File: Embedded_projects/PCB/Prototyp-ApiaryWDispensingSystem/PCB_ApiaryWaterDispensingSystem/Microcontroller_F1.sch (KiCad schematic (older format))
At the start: 47 parts, among them J4 Conn_01x06

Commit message: F1 completed
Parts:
- added C10: 20pF, symbol Device:C
- added J1, J4, J?: Conn_02x01, symbol Connector_Generic:Conn_02x01
- added JP16, JP? (x2): Jumper_2_Open, symbol Jumper:Jumper_2_Open
- added R2, R3: 10k, symbol Device:R
- added R23, R27, R4: 4k7, symbol Device:R
- added R24, R25: 100, symbol Device:R
- added R26: [N/A], symbol Device:R
- added R6: 100k, symbol Device:R
- added R7: 2k7, symbol Device:R
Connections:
- net +3V3: now also J1.1 (Pin_1), R23.1, R26.2
- net +5VA: now also R7.2
- net AIN_1: now also U?.10 (PA0), R23.2, R27.2
- net GND: now also U?.20 (PB2), U?.23 (VSS), U?.35 (VSS), U?.47 (VSS), U?.8 (VSSA), C10.2, J4.1 (Pin_1), R2.1, R27.1, R3.1, R4.1, R6.2
- net STM_JTCK: now also U?.37 (PA14)
- net STM_JTMS: now also U?.34 (PA13)
- net T_JTCK: now also U?.15 (PA5), U?.26 (PB13)
- net T_JTMS: now also U?.27 (PB14), R24.1
- net T_NRST: now also U?.18 (PB0)
- net T_SWO: now also U?.31 (PA10)
- net USB_DM: now also U?.32 (PA11)
- net USB_DP: now also U?.33 (PA12)
- net USB_RENUMn: now also U?.38 (PA15)
- net OSC_OUT: now reaches C?.2, U?.6 (PD1), Y?.1
- net OSC_IN: now reaches C3.2, U?.5 (PD0), Y?.2
- net ST_LINK_TX: now reaches U?.12 (PA2)
- net ST_LINK_TX: now also J?.1 (Pin_1), JP?.1 (A)
- net ST_LINK_RX: now reaches U?.13 (PA3)
- net ST_LINK_RX: now also J?.2 (Pin_2), JP?.1 (A)
- net T_JTDO: now reaches U?.16 (PA6)
- net T_JTDI: now reaches U?.17 (PA7)
- net at U?.2 (PC13): now also R3.2
- net at U?.21 (PB10): now also J4.2 (Pin_2), R26.1
- net T_SWDIO_IN: now reaches U?.25 (PB12)
- net T_SWDIO_IN: now also R24.2
- net PWR_ENn: now reaches U?.28 (PB15)
- net PWR_ENn: now also J1.2 (Pin_2), R4.2, R7.1
- net at U?.29 (PA8): now also R25.2
- net at U?.3 (PC14): now also R2.2
- net LED_STLINK: now reaches U?.30 (PA9)
- net PWR_EXT: now reaches U?.39 (PB3)
- net BOOT0: now reaches U?.44 (BOOT0)
- net BOOT0: now also R6.1
- new net: C10.1, JP16.1 (A), R25.1
- new net MCO: JP16.2 (B)
- new net STLK_RX: JP?.2 (B)
- new net STLK_TX: JP?.2 (B)
- no-connect marks 1 -> 11

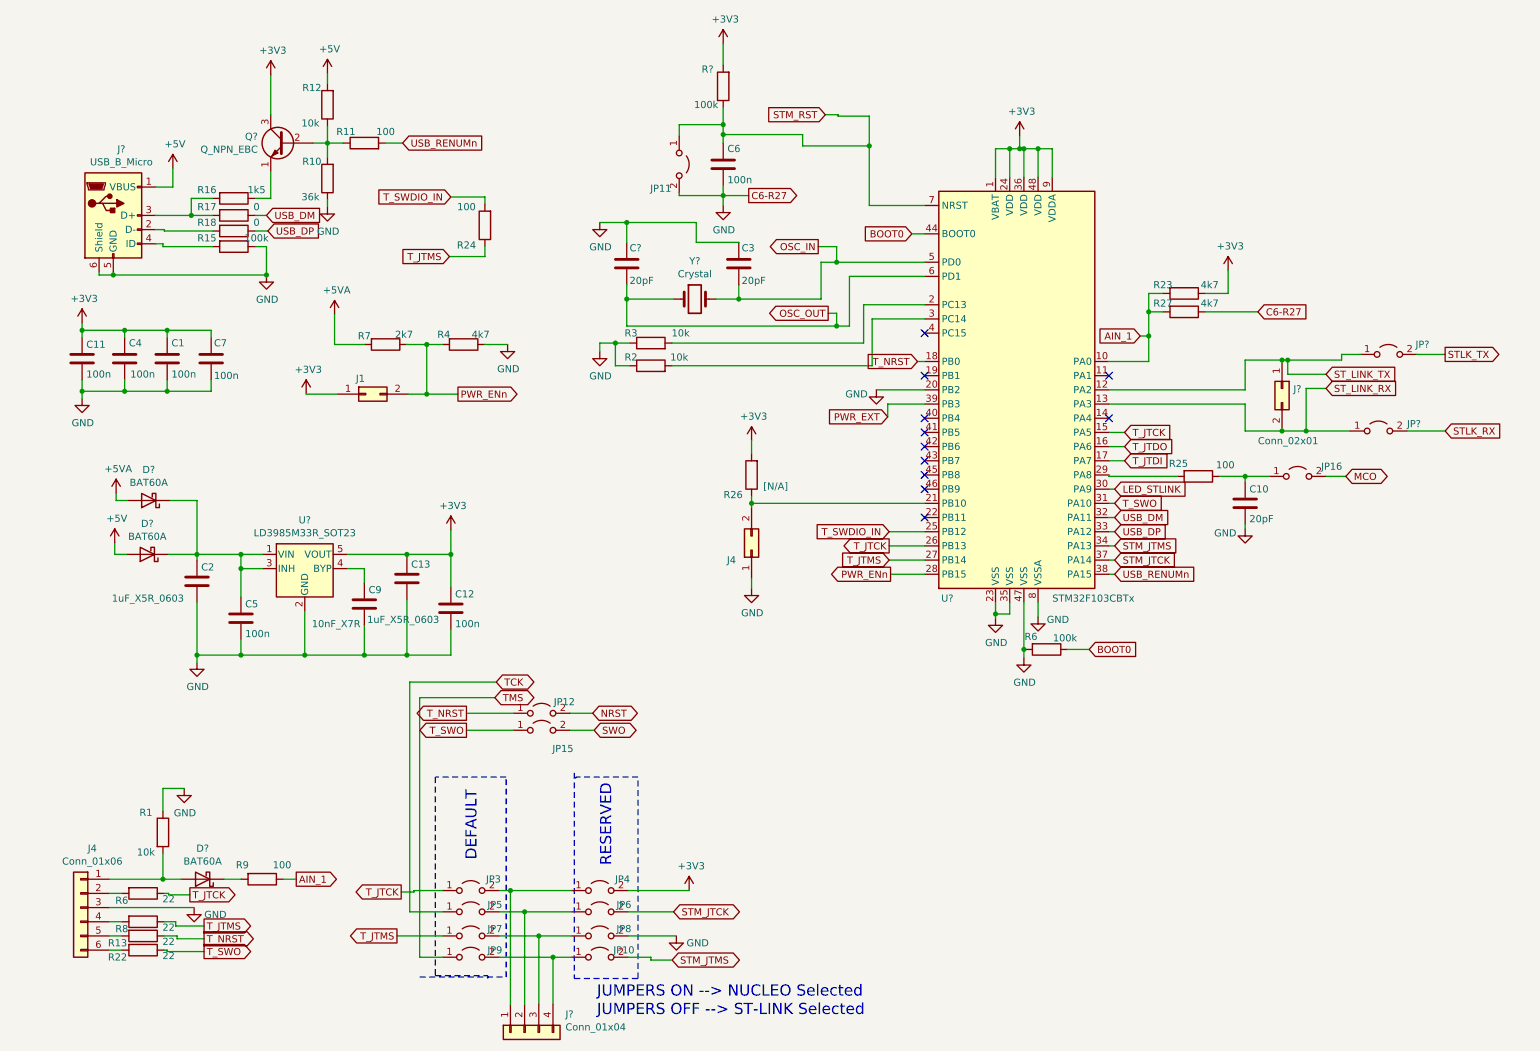
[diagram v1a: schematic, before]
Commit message: added changes of Microntroller_F4 ->global variables #3
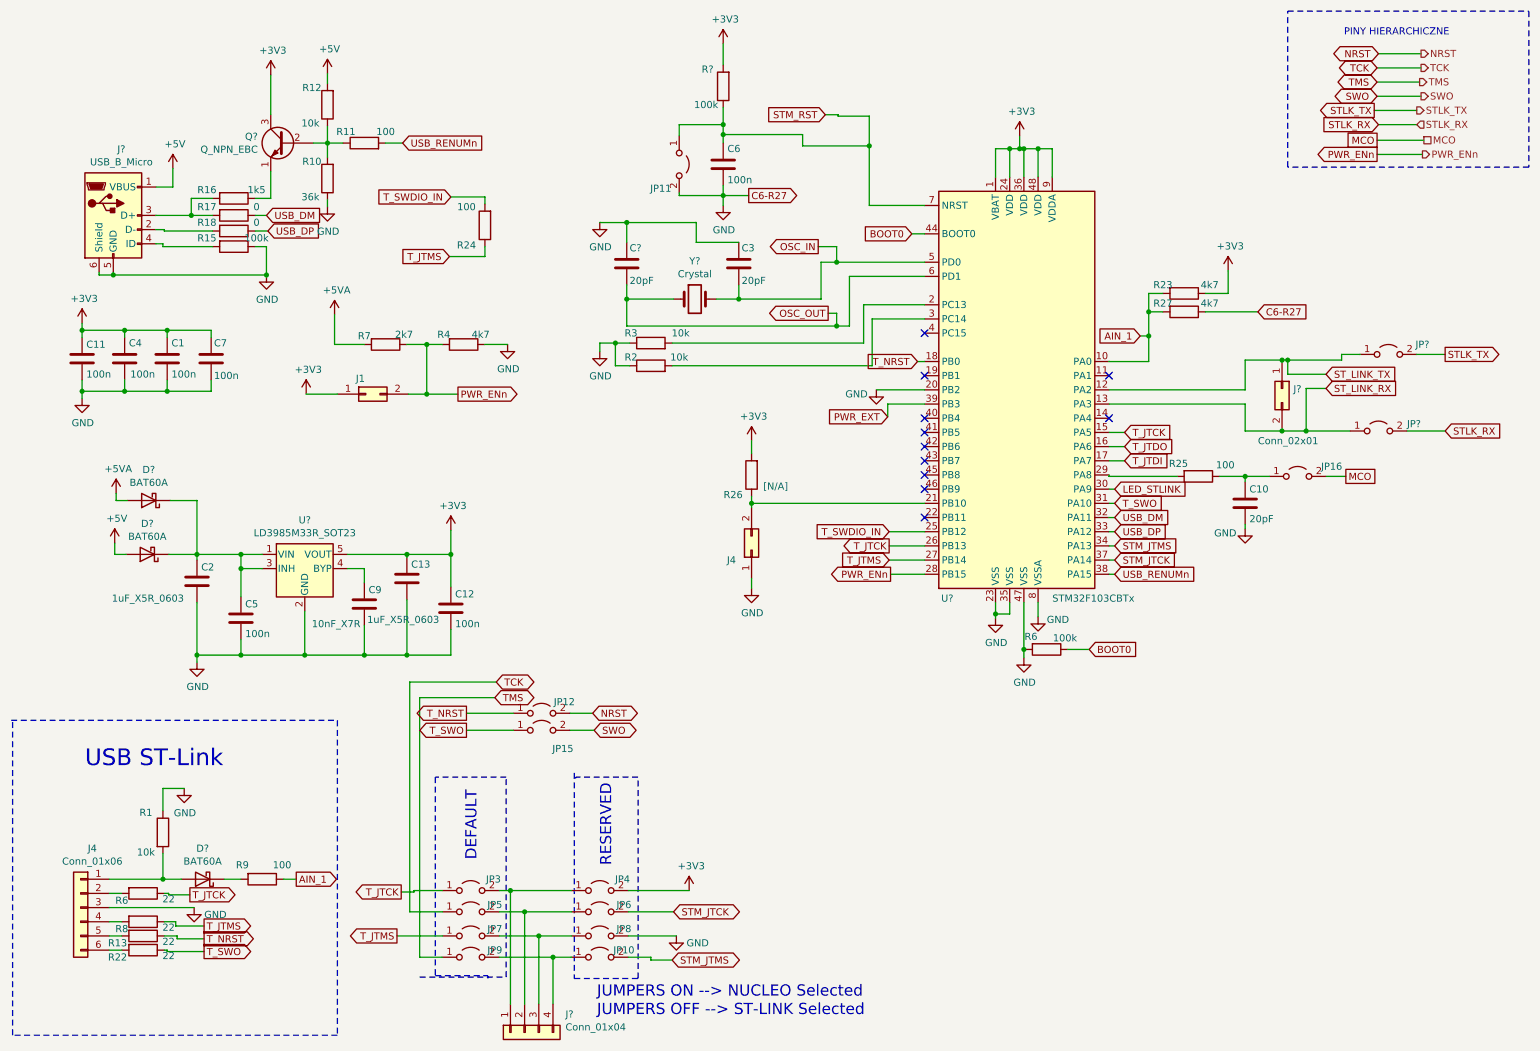
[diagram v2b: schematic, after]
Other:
- note added: "PINY HIERARCHICZNE"
- note added: "USB ST-Link"
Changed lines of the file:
@@
 Wire Wire Line
 	9200 4120 9200 4150
-Text GLabel 9910 3780 2    50   BiDi ~ 0
+Text GLabel 9910 3780 2    50   UnSpc ~ 0
 MCO
 Wire Wire Line
@@
 Wire Wire Line
 	7740 4770 7740 4670
+Text Notes 1020 5840 0    118  ~ 0
+USB ST-Link
+Wire Notes Line
+	500  5500 2800 5500
+Wire Notes Line
+	2800 5500 2800 7720
+Wire Notes Line
+	2800 7720 510  7720
+Wire Notes Line
+	510  7720 510  5500
+Text GLabel 10110 1200 0    50   Output ~ 0
+STLK_TX
+Text GLabel 10140 1300 0    50   Input ~ 0
+STLK_RX
+Text HLabel 10410 1200 2    50   Output ~ 0
+STLK_TX
+Text HLabel 10410 1300 2    50   Input ~ 0
+STLK_RX
+Wire Wire Line
+	10410 1200 10110 1200
+Wire Wire Line
+	10410 1300 10140 1300
+Text GLabel 10130 1410 0    50   UnSpc ~ 0
+MCO
+Text HLabel 10460 1410 2    50   UnSpc ~ 0
+MCO
+Wire Wire Line
+	10460 1410 10130 1410
+Text GLabel 10130 1510 0    50   Output ~ 0
+PWR_ENn
+Text HLabel 10450 1510 2    50   Output ~ 0
+PWR_ENn
+Wire Wire Line
+	10450 1510 10130 1510
+Text GLabel 10130 1000 0    50   BiDi ~ 0
+TMS
+Text GLabel 10130 900  0    50   BiDi ~ 0
+TCK
+Text GLabel 10140 800  0    50   BiDi ~ 0
+NRST
+Text GLabel 10130 1100 0    50   BiDi ~ 0
+SWO
+Text HLabel 10440 800  2    50   Output ~ 0
+NRST
+Text HLabel 10440 900  2    50   Output ~ 0
+TCK
+Text HLabel 10430 1000 2    50   Output ~ 0
+TMS
+Text HLabel 10440 1100 2    50   Output ~ 0
+SWO
+Wire Wire Line
+	10130 1100 10440 1100
+Wire Wire Line
+	10430 1000 10130 1000
+Wire Wire Line
+	10130 900  10440 900
+Wire Wire Line
+	10140 800  10440 800
+Text Notes 10640 680  2    50   ~ 0
+PINY HIERARCHICZNE
+Wire Notes Line
+	9500 500  11200 500
+Wire Notes Line
+	11200 500  11200 1600
+Wire Notes Line
+	11200 1600 9500 1600
+Wire Notes Line
+	9500 1600 9500 500
 $EndSCHEMATC

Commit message: added lot of changes to project #3
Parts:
- added LD?: LD_BICOLOR_CMS, symbol ApiaryWaterDispensingSystem:LD_BICOLOR_CMS
- added R19, R20, R21: 100, Resistor_SMD:R_0805_2012Metric, symbol Device:R
- C1, C10, C11, C12, C3, C4, C5, C6, C7, R24: footprint (none) -> Capacitor_SMD:C_0805_2012Metric
- C13, C2, C9: footprint (none) -> Capacitor_SMD:C_0603_1608Metric
- C8: renamed from C?; footprint (none) -> Capacitor_SMD:C_0805_2012Metric
- J1, J4, J?: footprint (none) -> Connector_PinHeader_2.54mm:PinHeader_1x02_P2.54mm_Vertical
- J4: footprint (none) -> Connector_PinHeader_2.54mm:PinHeader_1x06_P2.54mm_Vertical
- J?: footprint (none) -> Connector_USB:USB_Mini-B_Lumberg_2486_01_Horizontal
- J?: footprint (none) -> Connector_PinHeader_2.54mm:PinHeader_1x04_P2.54mm_Vertical
- JP10, JP11, JP12, JP15, JP16, JP3, JP4, JP5, JP6, JP7, JP8, JP9: footprint (none) -> Jumper:SolderJumper-2_P1.3mm_Open_TrianglePad1.0x1.5mm
- JP13, JP14: renamed from JP?; footprint (none) -> Jumper:SolderJumper-2_P1.3mm_Open_TrianglePad1.0x1.5mm
- R1, R10, R11, R12, R13, R15, R16, R17, R18, R2, R22, R23, R25, R26, R27, R3, R4, R6, R7, R8, R9, R?: footprint (none) -> Resistor_SMD:R_0805_2012Metric
- X1: renamed from Y?; footprint (none) -> Crystal:Resonator-2Pin_W8.0mm_H3.5mm
- gave numbers to parts that had none: 3
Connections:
- net +3V3: now also R19.2
- net GND: now also C8.2, LD?.1; no longer C8.1
- net LED_STLINK: now also R20.1, R21.1
- net OSC_IN: now also X1.1; no longer X1.2
- net OSC_OUT: now also C8.1, X1.2; no longer C8.2, X1.1
- net +5V renamed +5VP
- new net: LD?.2, R21.2
- new net: LD?.3, R20.2
- new net: LD?.4, R19.1
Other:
- note added: "PWR"
- moved on the sheet: C3, C8, X1

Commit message: Many design changes have been added over the past few months #3
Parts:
- added J11, J12: Conn_02x01, Connector_PinHeader_2.54mm:PinHeader_1x02_P2.54mm_Vertical, symbol Connector_Generic:Conn_02x01
- C1, C10, C11, C12, C3, C4, C5, C6, C7, C8, R24: footprint Capacitor_SMD:C_0805_2012Metric -> Capacitor_SMD:C_0603_1608Metric
- R1, R10, R11, R12, R13, R15, R16, R17, R18, R19, R2, R20, R21, R22, R23, R25, R26, R27, R3, R4, R6, R7, R8, R9, R?: footprint Resistor_SMD:R_0805_2012Metric -> Resistor_SMD:R_0603_1608Metric
- R5: renamed from R6; footprint Resistor_SMD:R_0805_2012Metric -> Resistor_SMD:R_0603_1608Metric
- gave numbers to parts that had none: 2
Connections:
- net GND: now also J11.1 (Pin_1), J11.2 (Pin_2), J12.1 (Pin_1), J12.2 (Pin_2)
- net PWR_ENn: no longer J1.2 (Pin_2), R4.2, R7.1
- net PWR_EXT: now also J1.2 (Pin_2), R4.2, R7.1
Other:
- note added: "Wired on Solder Side"
- note added: "good"

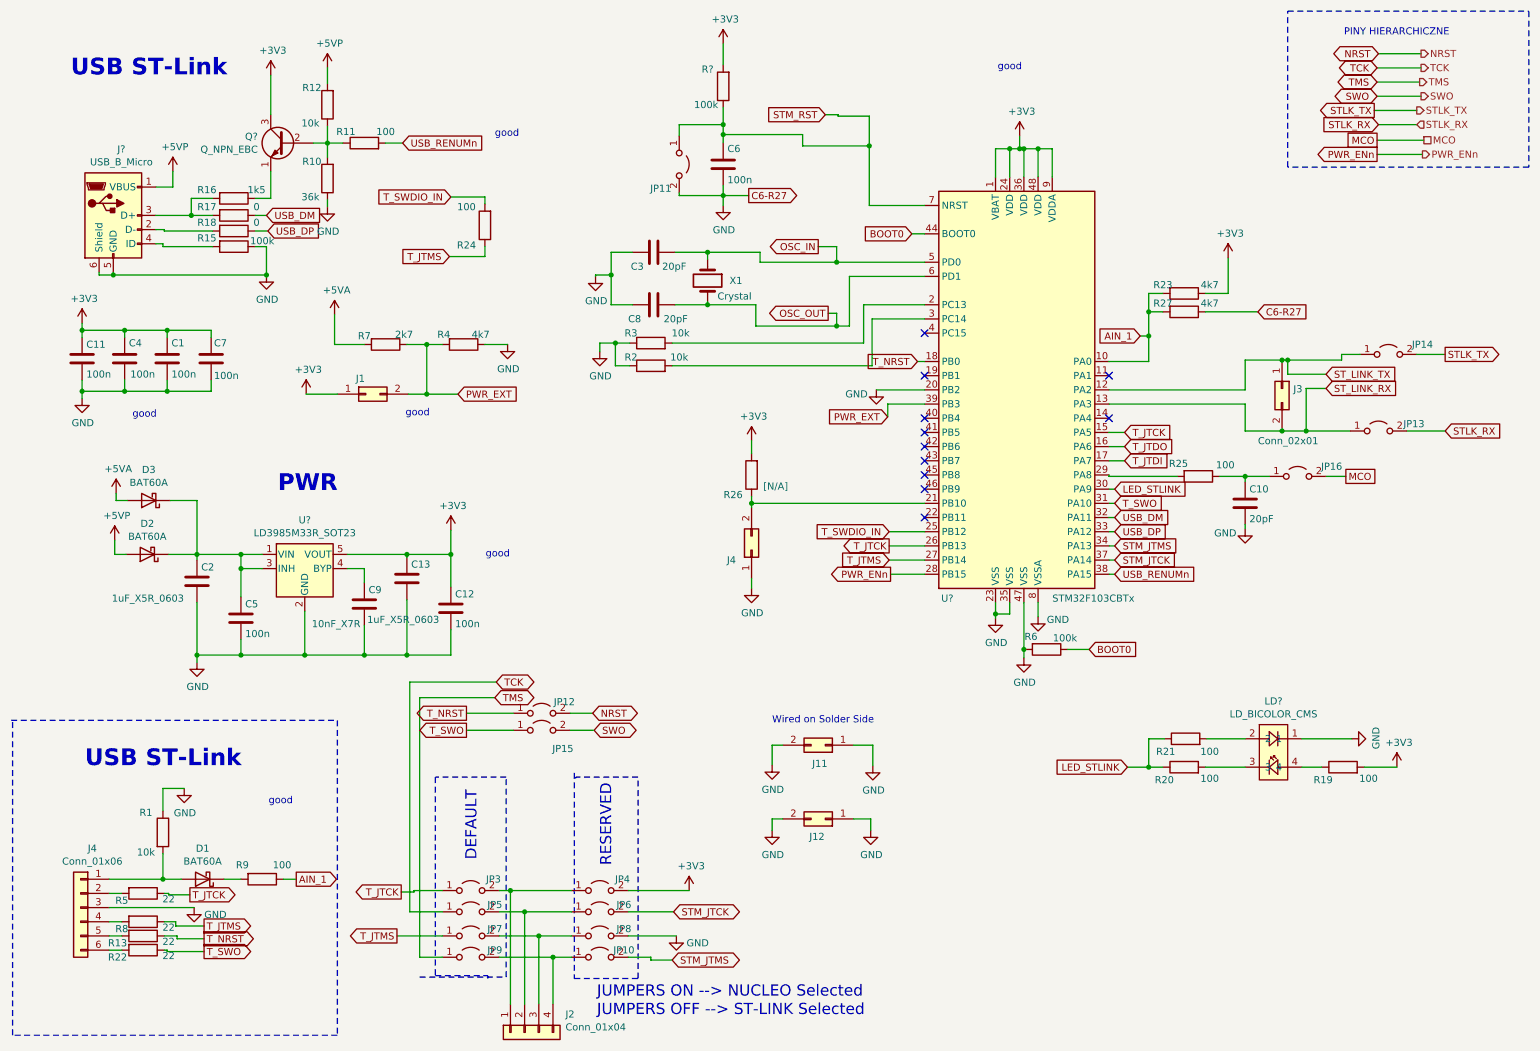
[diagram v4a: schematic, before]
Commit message: All signal has been routed, the analog part needs to be completed
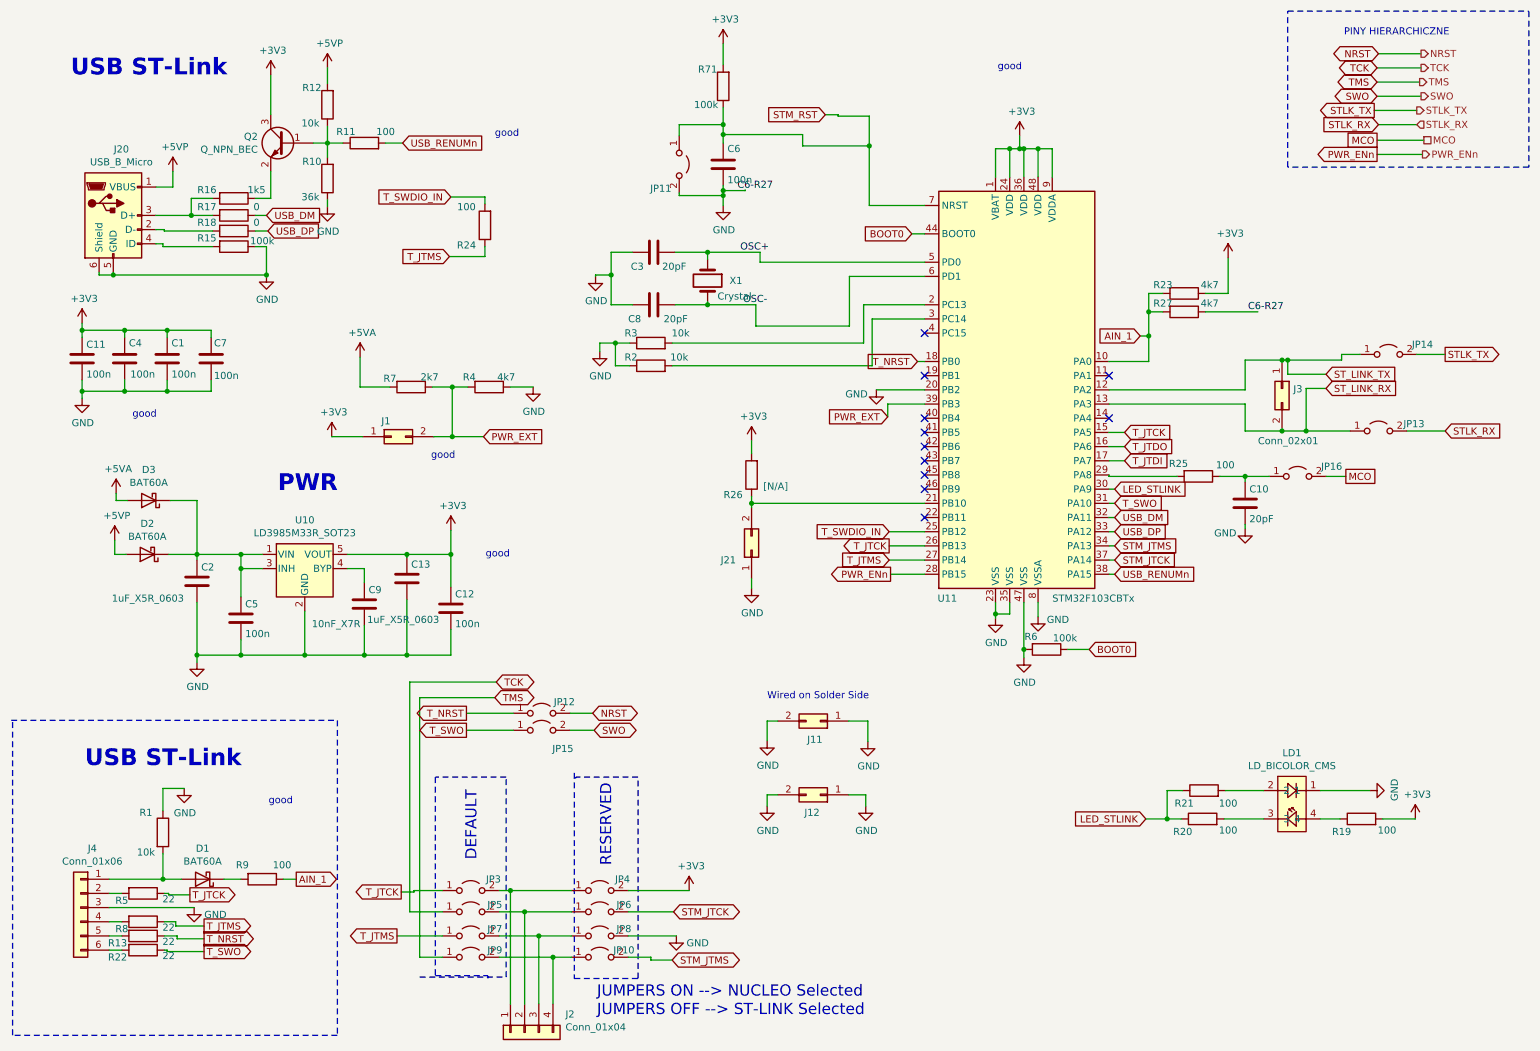
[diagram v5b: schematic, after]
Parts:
- removed Q?: Q_NPN_EBC, symbol Device:Q_NPN_EBC
- added Q2: Q_NPN_BEC, Package_TO_SOT_SMD:SOT-23, symbol Device:Q_NPN_BEC
- LD1: renamed from LD?; footprint (none) -> ApiaryWaterDispensingSystem:LD_BiCOLOR_CMS
- gave numbers to parts that had none: 4
- renumbered J4 to J21
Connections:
- net +3V3: now also Q2.3 (C)
- net at R16.1: now also Q2.2 (E)
- net at R10.2, R11.1, R12.1: now also Q2.1 (B)
- net OSC_IN renamed OSC+
- net OSC_OUT renamed OSC-
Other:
- moved on the sheet: J1, J11, J12, LD1, R19, R20, R21, R4, R7
